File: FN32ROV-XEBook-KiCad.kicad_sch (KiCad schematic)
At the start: 39 parts, among them J2 USB-C 16P, U1 ESP32-WROVER-E, U2 CP2102N-A02-GQFN24R, U3 74LS07DR, U4 74LS07DR

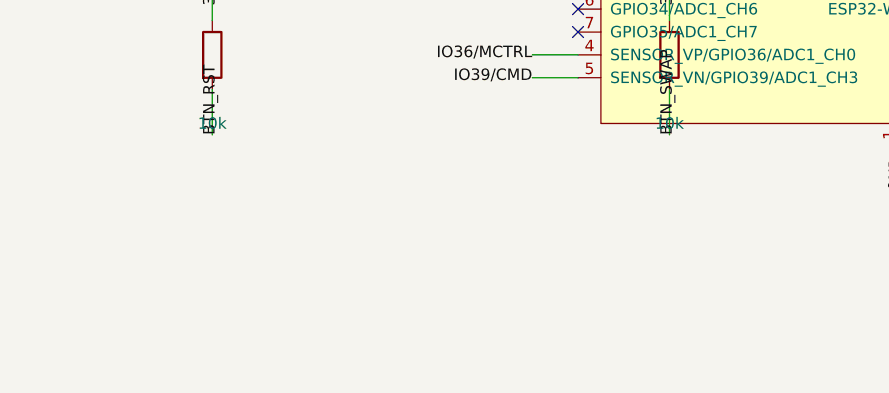
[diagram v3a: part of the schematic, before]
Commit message: Wire up the USB auto-reset transistor circuit (Q1)
Places Q1 (UMH3N dual-transistor) using the exact pinout from ROHM's
datasheet (Datasheets/UMH3NTN.pdf): DTr1 (RTS -> EN) and DTr2 (DTR ->
GPIO0/BTN_SWAP), each transistor placed as its own unit instance since
the KiCad symbol models the package the same way as the 74xx gates —
one placeable unit per transistor sharing a reference designator.
Adds the EN pullup (R5) and decoupling cap (C2).

This resolves the deferred ambiguity from the previous commit — the
datasheet's inner-circuit diagram made the base/collector/emitter
assignment unambiguous. RTS/DTR/EN are no longer dangling nets, and
U1's EN pin is no longer undriven. ERC is down to 7 violations, all
expected (power switch path and the 3.3V regulator, both still
unbuilt).

Co-Authored-By: Claude Sonnet 5 <noreply@anthropic.com>
Claude-Session: https://claude.ai/code/session_01ATUvQCobb1cVELUyjLrcQZ
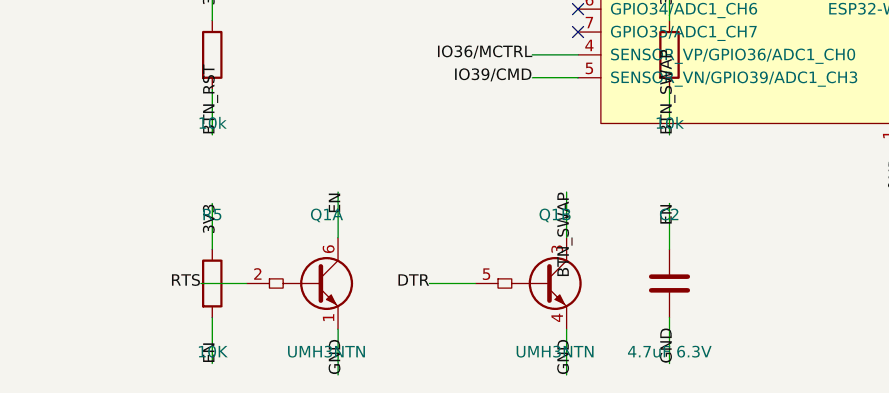
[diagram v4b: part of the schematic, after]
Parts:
- added C2: 4.7uF 6.3V, Capacitor_SMD:C_0402_1005Metric, symbol Device:C
- added Q1: UMH3NTN, Package_TO_SOT_SMD:SOT-363_SC-70-6, symbol Transistor_BJT:Q_Dual_NPN_NPN_BRT_No_R2_E1B1C2E2B2C1
- added R5: 10K, Resistor_SMD:R_0402_1005Metric, symbol Device:R
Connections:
- net 3V3: now also R5.1
- net BTN_SWAP: now also Q1.3 (C2)
- net DTR: now also Q1.5 (B2)
- net EN: now also C2.1, Q1.6 (C1), R5.2
- net GND: now also C2.2, Q1.1 (E1), Q1.4 (E2)
- net RTS: now also Q1.2 (B1)

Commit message: Complete the power path and SD bus pullups — schematic capture done
Wires up the remaining retained circuitry: the diode-ORed VCC input
(D7/D8 from USB_5V/SIO_5V), the XC6220B331MR 3.3V regulator with its
J_PWR-driven enable line (replacing the original onboard slide
switch), the Q2/Q3 MOSFET pair forming an always-enabled ideal-diode
power switch to VCC_BUF, and the six pullup resistors on the SD card's
SPI bus (including DAT1/DAT2, which needed their own pullup nets
rather than being left unconnected as I'd assumed earlier).

Adds PWR_FLAG markers on the externally-fed root supply nets (GND,
USB_5V, SIO_5V, PWR_SW_VCC) so ERC recognizes them as legitimately
driven from off-board sources rather than flagging every downstream
power pin.

ERC is down to a single violation: IO12/TDI, a spare/unused test point
in the original design with nothing else to connect to. This completes
the schematic capture of FN32ROV-1.7.1's retained circuitry, matched
pin-by-pin against the original DipTrace schematic image and (for Q1)
the ROHM UMH3NTN datasheet. Next: footprints, then PCB layout.

Co-Authored-By: Claude Sonnet 5 <noreply@anthropic.com>
Claude-Session: https://claude.ai/code/session_01ATUvQCobb1cVELUyjLrcQZ
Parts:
- added C10, C11: 4.7uF 6.3V, Capacitor_SMD:C_0402_1005Metric, symbol Device:C
- added C12: 4.7uF 10V, Capacitor_SMD:C_0402_1005Metric, symbol Device:C
- added D7, D8: PMEG2010ER,115, Diode_SMD:D_SOD-323, symbol Device:D
- added Q2: DMP2035U-7, Package_TO_SOT_SMD:SOT-23, symbol Device:Q_PMOS
- added Q3: DMG2302U, Package_TO_SOT_SMD:SOT-23, symbol Device:Q_NMOS
- added R17, R18, R19, R20, R23, R27, R28: 10K, Resistor_SMD:R_0402_1005Metric, symbol Device:R
- added R21: 1k, Resistor_SMD:R_0402_1005Metric, symbol Device:R
- added R22: 10k, Resistor_SMD:R_0402_1005Metric, symbol Device:R
- added U5: XC6220B331MR, Package_TO_SOT_SMD:SOT-23-5, symbol Regulator_Linear:XC6220B331MR
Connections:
- net 3V3: now also C11.1, R17.2, R18.2, R19.2, R21.1, R23.2, R27.2, R28.2, U5.5 (VOUT)
- net GND: now also C10.2, C11.2, C12.2, Q3.S, R22.2, U5.2 (GND)
- net IO15/TDO: now also R23.1
- net IO19/SPI_MISO: now also R17.1
- net IO23/SPI_MOSI: now also R18.1
- net IO5/SPI_CS: now also R19.1
- net PWR_SW_EN: now also R22.1, U5.3 (CE)
- net PWR_SW_VCC: now also C10.1, D7.1 (K), D8.1 (K), Q2.S, R20.2, U5.1 (VIN)
- net SIO_5V: now also C12.1, D8.2 (A)
- net USB_5V: now also D7.2 (A)
- net VCC_BUF: now also Q2.D
- net SD_DAT2: now reaches SD1.1 (DAT2)
- net SD_DAT2: now also R28.1
- net SD_DAT1: now reaches SD1.8 (DAT1)
- net SD_DAT1: now also R27.1
- new net Q2_GATE: Q2.G, Q3.D, R20.1
- new net Q3_GATE: Q3.G, R21.2
- no-connect marks 25 -> 24

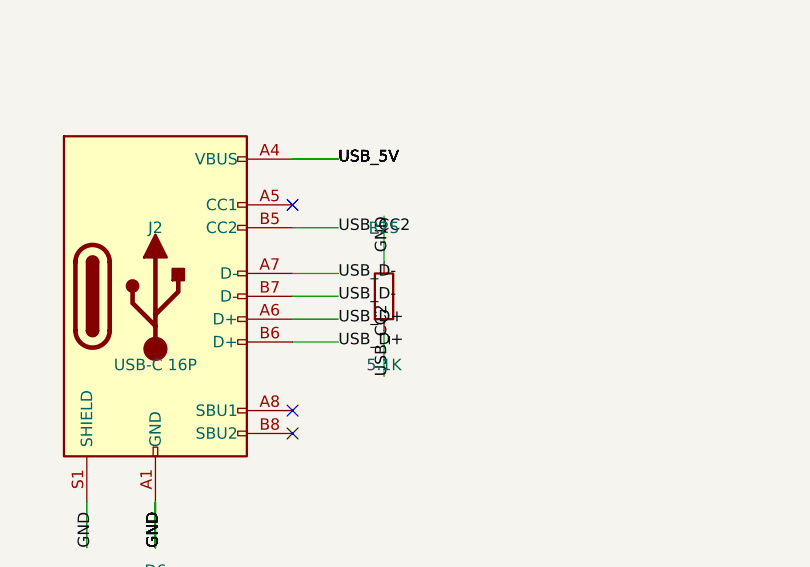
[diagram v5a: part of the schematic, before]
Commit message: Fix missed R26 (second USB-C CC pulldown) and reconcile against BOM
R26 is a 5.1K pulldown on CC1, mirroring R25 on CC2 — a fully
spec-compliant dual-CC-pulldown USB-C sink, not the asymmetric CC1-NC
setup I'd concluded earlier from a crop that didn't extend far enough
left to show CC1's actual wire routing. Caught by re-checking the
original DipTrace file directly.

Also ran a full reconciliation of every BOM reference designator
against what's placed in the KiCad schematic, to catch anything else
missed the same way. Everything is now accounted for: BOM items are
either placed directly, or intentionally relocated to the new JST/IDC
connectors (D1-D3 LEDs, S1/S2/S4/S5 switches, J1/J3 SIO connectors),
with R29 excluded since it's BOM-marked "NOSTUFF" (never populated).

ERC remains at the single expected violation (IO12/TDI, unused test
point).

Co-Authored-By: Claude Sonnet 5 <noreply@anthropic.com>
Claude-Session: https://claude.ai/code/session_01ATUvQCobb1cVELUyjLrcQZ
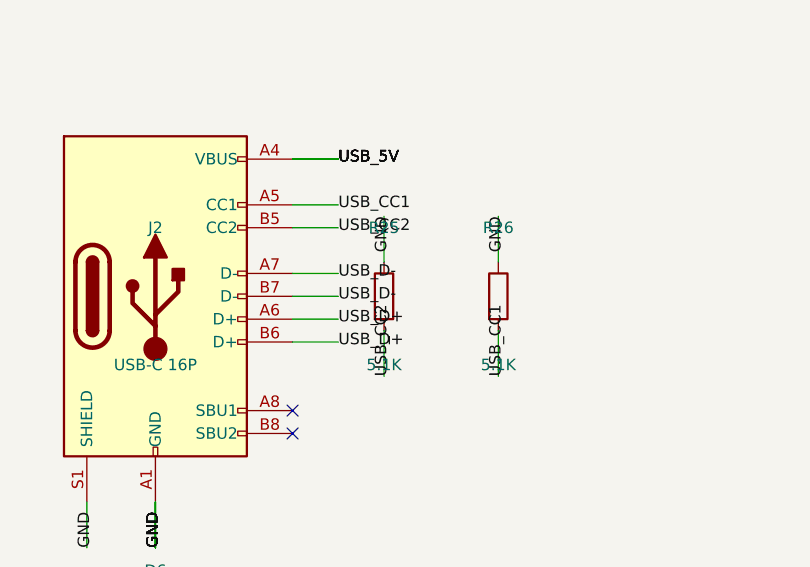
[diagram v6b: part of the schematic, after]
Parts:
- added R26: 5.1K, Resistor_SMD:R_0402_1005Metric, symbol Device:R
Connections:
- net GND: now also R26.1
- net USB_CC1: now reaches J2.A5 (CC1)
- net USB_CC1: now also R26.2
- no-connect marks 24 -> 23
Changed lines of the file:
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@@
 		)
 	)
-	(no_connect
-		(at 523.24 243.84)
+	(wire
+		(pts
+			(xy 523.24 243.84) (xy 528.32 243.84)
+		)
+		(stroke
+			(width 0)
+			(type solid)
+		)
+	)
+	(label "USB_CC1"
+		(at 528.32 243.84 0)
+		(effects
+			(font
+				(size 1.27 1.27)
+			)
+			(justify left)
+		)
 	)
 	(wire
@@
 		(effects
 			(font
+				(size 1.27 1.27)
+			)
+			(justify left)
+		)
+	)
+	(symbol
+		(lib_id "Device:R")
+		(at 546.1 254 0)
+		(unit 1)
+		(exclude_from_sim no)
+		(in_bom yes)
+		(on_board yes)
+		(dnp no)
+		(property "Reference" "R26"
+			(at 546.1 246.38 0)
+			(effects
+				(font
+					(size 1.27 1.27)
+				)
+			)
+		)
+		(property "Value" "5.1K"
+			(at 546.1 261.62 0)
+			(effects
+				(font
+					(size 1.27 1.27)
+				)
+			)
+		)
+		(property "Footprint" "Resistor_SMD:R_0402_1005Metric"
+			(at 546.1 254 0)
+			(effects
+				(font
+					(size 1.27 1.27)
+				)
+				(hide yes)
+			)
+		)
+		(property "Datasheet" "~"
+			(at 546.1 254 0)
+			(effects
+				(font
+					(size 1.27 1.27)
+				)
+				(hide yes)
+			)
+		)
+		(pin "1"
+		)
+		(pin "2"
+		)
+		(instances
+			(project "FN32ROV-XEBook-KiCad"
+				(path "/4c3930ed-aadd-48ff-beab-e5d9c5d47b74"
+					(reference "R26")
+					(unit 1)
+				)
+			)
+		)
+	)
+	(wire
+		(pts
+			(xy 546.1 250.19) (xy 546.1 245.11)
+		)
+		(stroke
+			(width 0)
+			(type solid)
+		)
+	)
+	(label "GND"
+		(at 546.1 245.11 270)
+		(effects
+			(font
+				(size 1.27 1.27)
+			)
+			(justify right)
+		)
+	)
+	(wire
+		(pts
+			(xy 546.1 257.81) (xy 546.1 262.89)
+		)
+		(stroke
+			(width 0)
+			(type solid)
+		)
+	)
+	(label "USB_CC1"
+		(at 546.1 262.89 90)
+		(effects
+			(font

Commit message: Fix real wiring errors found via ground-truth netlist comparison
The user exported DipTrace's actual netlist (KiCad-format, since
DipTrace 5+ supports it) and I diffed it against this project's own
exported netlist. That comparison — matching every (ref, pin) against
the ground truth rather than trusting my visual reading of the
schematic image — found genuine errors beyond the R26 miss:

- Q1 was wired backwards. The real auto-reset circuit cross-couples
  each transistor's emitter to the *other* control signal (E1->RTS,
  B1->DTR, E2->DTR, B2->RTS), not to GND as I'd derived from the
  datasheet's generic inner-circuit diagram.
- U2's VIO/VDD pins are on their own isolated VDD net — the CP2102N
  generates VDD internally from VREGIN, so merging it into USB_5V was
  wrong. Fixed R10's pullup and C4/C5's decoupling to match.
- R4/R7 (SIO_5V presence sense, read via U1 GPIO35/"IO35") and R8/C3
  (ESP32 DAC1 -> SIO_AUDIOIN coupling, via U1 GPIO25) are two entirely
  separate, unrelated circuits that I'd incorrectly merged into one
  "BTN_BT" node along with R1's actual ButtonB sense line.
- U1 pin 6 (GPIO34) is ButtonB's real read pin and was left
  unconnected.

Verified with kicad-cli's ERC (1 expected violation: IO12/TDI, unused
test point) and a full netlist diff against the DipTrace export,
cross-checked both by (ref,pin) number and by pin function name to
rule out any remaining discrepancy. The reference netlist is now
committed under reference/ for future verification passes.

Co-Authored-By: Claude Sonnet 5 <noreply@anthropic.com>
Claude-Session: https://claude.ai/code/session_01ATUvQCobb1cVELUyjLrcQZ
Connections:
- net BTN_BT: now also U1.6 (GPIO34/ADC1_CH6); no longer R4.2, R7.2, R8.2
- net CP2102_RESET: now also R10.1; no longer R10.2
- net DTR: now also Q1.2 (B1), Q1.4 (E2); no longer Q1.5 (B2)
- net GND: no longer Q1.1 (E1), Q1.4 (E2)
- net RTS: now also Q1.1 (E1), Q1.5 (B2); no longer Q1.2 (B1)
- net USB_5V: no longer C4.2, C5.2, R10.1, U2.5 (VIO), U2.6 (VDD)
- net IO25_DAC: now reaches U1.10 (DAC_1/ADC2_CH8/GPIO25)
- net IO25_DAC: now also R8.2
- net IO35: now reaches U1.7 (GPIO35/ADC1_CH7)
- net IO35: now also R4.2, R7.2
- new net VDD: C4.2, C5.2, R10.2, U2.5 (VIO), U2.6 (VDD)
- no-connect marks 23 -> 20
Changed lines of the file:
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@@
 		)
 	)
-	(no_connect
-		(at 91.44 261.62)
+	(wire
+		(pts
+			(xy 91.44 261.62) (xy 86.36 261.62)
+		)
+		(stroke
+			(width 0)
+			(type solid)
+		)
 	)
-	(no_connect
-		(at 91.44 264.16)
+	(label "BTN_BT"
+		(at 86.36 261.62 180)
+		(effects
+			(font
+				(size 1.27 1.27)
+			)
+			(justify right)
+		)
+	)
+	(wire
+		(pts
+			(xy 91.44 264.16) (xy 86.36 264.16)
+		)
+		(stroke
+			(width 0)
+			(type solid)
+		)
+	)
+	(label "IO35"
+		(at 86.36 264.16 180)
+		(effects
+			(font
+				(size 1.27 1.27)
+			)
+			(justify right)
+		)
 	)
 	(wire
@@
 		)
 	)
-	(no_connect
-		(at 162.56 266.7)
+	(wire
+		(pts
+			(xy 162.56 266.7) (xy 167.64 266.7)
+		)
+		(stroke
+			(width 0)
+			(type solid)
+		)
+	)
+	(label "IO25_DAC"
+		(at 167.64 266.7 0)
+		(effects
+			(font
+				(size 1.27 1.27)
+			)
+			(justify left)
+		)
 	)
 	(wire
@@
 		)
 	)
-	(label "BTN_BT"
+	(label "IO35"
 		(at 50.8 199.39 90)
 		(effects
@@
 		)
 	)
-	(label "BTN_BT"
+	(label "IO35"
 		(at 101.6 199.39 90)
 		(effects
@@
 		)
 	)
-	(label "BTN_BT"
+	(label "IO25_DAC"
 		(at 50.8 237.49 90)
 		(effects
@@
 		)
 	)
-	(label "USB_5V"
+	(label "VDD"
 		(at 457.2 220.98 270)
 		(effects
@@
 		)
 	)
-	(label "USB_5V"
+	(label "VDD"
 		(at 459.74 220.98 270)
 		(effects
@@
 		)
 	)
-	(label "USB_5V"
+	(label "CP2102_RESET"
 		(at 406.4 219.71 270)
 		(effects
@@
 		)
 	)
-	(label "CP2102_RESET"
+	(label "VDD"
 		(at 406.4 237.49 90)
 		(effects
@@
 		)
 	)
-	(label "USB_5V"
+	(label "VDD"
 		(at 431.8 237.49 90)
 		(effects
@@
 		)
 	)
-	(label "USB_5V"
+	(label "VDD"
 		(at 444.5 237.49 90)
 		(effects
@@
 		)
 	)
-	(label "RTS"
+	(label "DTR"
 		(at 49.53 292.1 180)
 		(effects
@@
 		)
 	)
-	(label "GND"
+	(label "RTS"
 		(at 64.77 302.26 90)
 		(effects
@@
 		)
 	)
-	(label "DTR"
+	(label "RTS"
 		(at 74.93 292.1 180)
 		(effects
@@
 		)
 	)
-	(label "GND"
+	(label "DTR"
 		(at 90.17 302.26 90)
 		(effects
@@
 		(effects
 			(font
+				(size 1.27 1.27)
+			)
+			(justify left)
+		)
+	)
+	(symbol
+		(lib_id "power:PWR_FLAG")
+		(at 647.7 175.26 0)
+		(unit 1)
+		(exclude_from_sim no)
+		(in_bom yes)
+		(on_board yes)
+		(dnp no)
+		(property "Reference" "#FLG6"
+			(at 647.7 167.64 0)
+			(effects
+				(font
+					(size 1.27 1.27)
+				)
+			)
+		)
+		(property "Value" "PWR_FLAG"
+			(at 647.7 182.88 0)
+			(effects
+				(font
+					(size 1.27 1.27)
+				)
+			)
+		)
+		(property "Footprint" ""
+			(at 647.7 175.26 0)
+			(effects
+				(font
+					(size 1.27 1.27)
+				)
+				(hide yes)
+			)
+		)
+		(property "Datasheet" "~"
+			(at 647.7 175.26 0)
+			(effects
+				(font
+					(size 1.27 1.27)
+				)
+				(hide yes)
+			)
+		)
+		(pin "1"
+		)
+		(instances
+			(project "FN32ROV-XEBook-KiCad"
+				(path "/4c3930ed-aadd-48ff-beab-e5d9c5d47b74"
+					(reference "#FLG6")
+					(unit 1)
+				)
+			)
+		)
+	)
+	(label "VDD"
+		(at 647.7 175.26 0)
+		(effects
+			(font

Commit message: Fix missing 3D models in footprints
Two gaps found after opening the assembled schematic/PCB in real KiCad:
the ESP32-WROVER-E footprint pointed at ${KICAD8_3RD_PARTY}, an env var
that's only populated when a library is installed via KiCad's Plugin
and Content Manager — since this one was fetched manually via curl, the
variable was never set and the model silently failed to resolve.

- Downloaded the real ESP32-WROVER-E .step/.wrl models from Espressif's
  kicad-libraries repo and repointed the footprint at them via
  ${KIPRJMOD}, which always resolves for anyone who clones the repo.
- The stock IDC-Header_2x06_P2.54mm_Latch_Horizontal and
  USB_C_Receptacle_HCTL_HC-TYPE-C-16P-01A footprints genuinely ship
  without bundled 3D models in KiCad's own library. Added local
  LocalOverrides.pretty copies pointing at visually-matching sibling
  models via KiCad's built-in ${KICAD9_3DMODEL_DIR}, and updated
  fp-lib-table plus the J_SIO/J2 generator scripts to use them.

Reassembled and re-verified the full schematic: ERC still clean (1
expected violation, IO12/TDI test point), and the footprint list no
longer shows the old Connector_IDC/Connector_USB stock references.

Co-Authored-By: Claude Sonnet 5 <noreply@anthropic.com>
Claude-Session: https://claude.ai/code/session_01ATUvQCobb1cVELUyjLrcQZ
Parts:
- J2: footprint Connector_USB:USB_C_Receptacle_HCTL_HC-TYPE-C-16P-01A -> LocalOverrides:USB_C_Receptacle_HCTL_HC-TYPE-C-16P-01A
- J_SIO: footprint Connector_IDC:IDC-Header_2x06_P2.54mm_Latch_Horizontal -> LocalOverrides:IDC-Header_2x06_P2.54mm_Latch_Horizontal
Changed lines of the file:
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@@
 			)
 		)
-		(property "Footprint" "Connector_IDC:IDC-Header_2x06_P2.54mm_Latch_Horizontal"
+		(property "Footprint" "LocalOverrides:IDC-Header_2x06_P2.54mm_Latch_Horizontal"
 			(at 50.8 50.8 0)
 			(effects
@@
 			)
 		)
-		(property "Footprint" "Connector_USB:USB_C_Receptacle_HCTL_HC-TYPE-C-16P-01A"
+		(property "Footprint" "LocalOverrides:USB_C_Receptacle_HCTL_HC-TYPE-C-16P-01A"
 			(at 508 254 0)
 			(effects
